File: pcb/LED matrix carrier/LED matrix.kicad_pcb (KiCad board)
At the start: 2 copper layers, 76.1 x 76.1 mm, 14 parts, among them J1 Conn_01x15_Pin, J2 Conn_01x15_Socket, J3 Conn_01x02_Pin, J4 Conn_01x02_Socket, J5 Conn_01x08_Socket, J6 Conn_01x08_Socket, J7 Conn_01x08_Socket, J8 Conn_01x08_Socket, U1 74HC594, U2 74HC594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

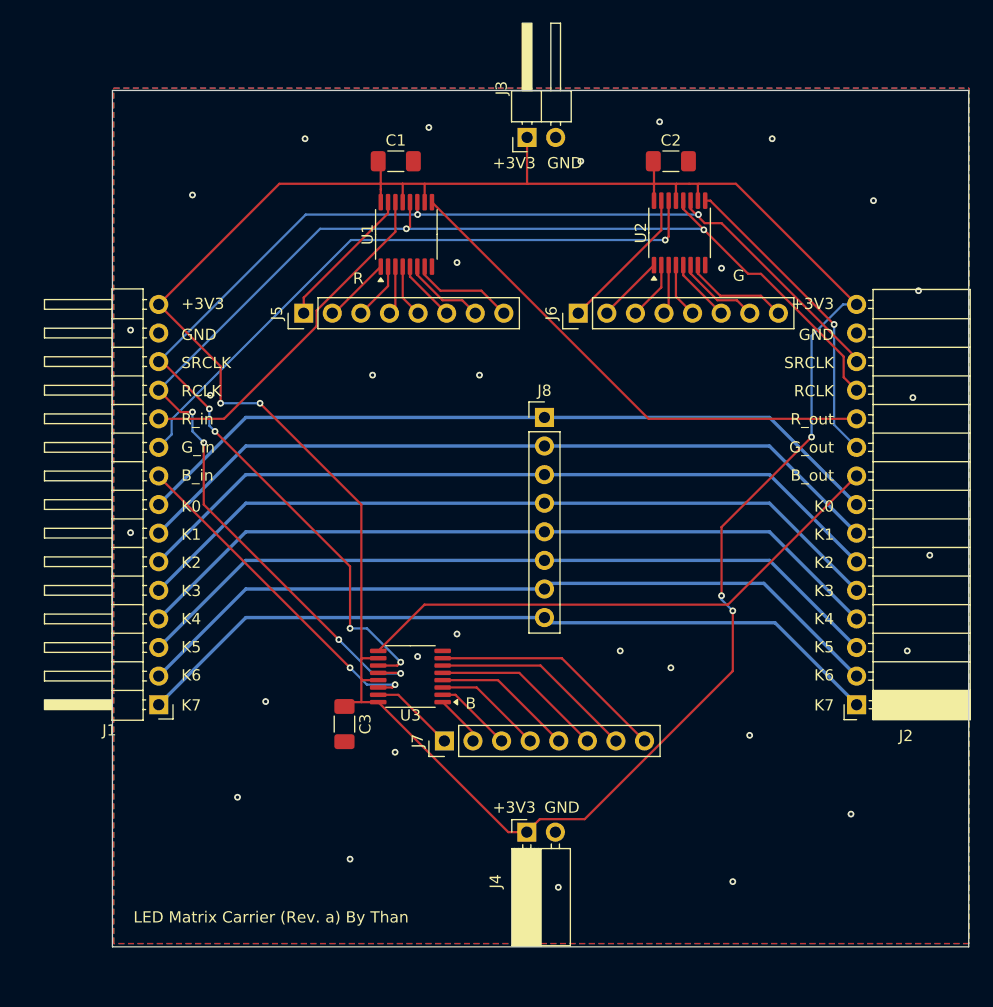
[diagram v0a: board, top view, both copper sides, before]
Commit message: export carrier pcb step model
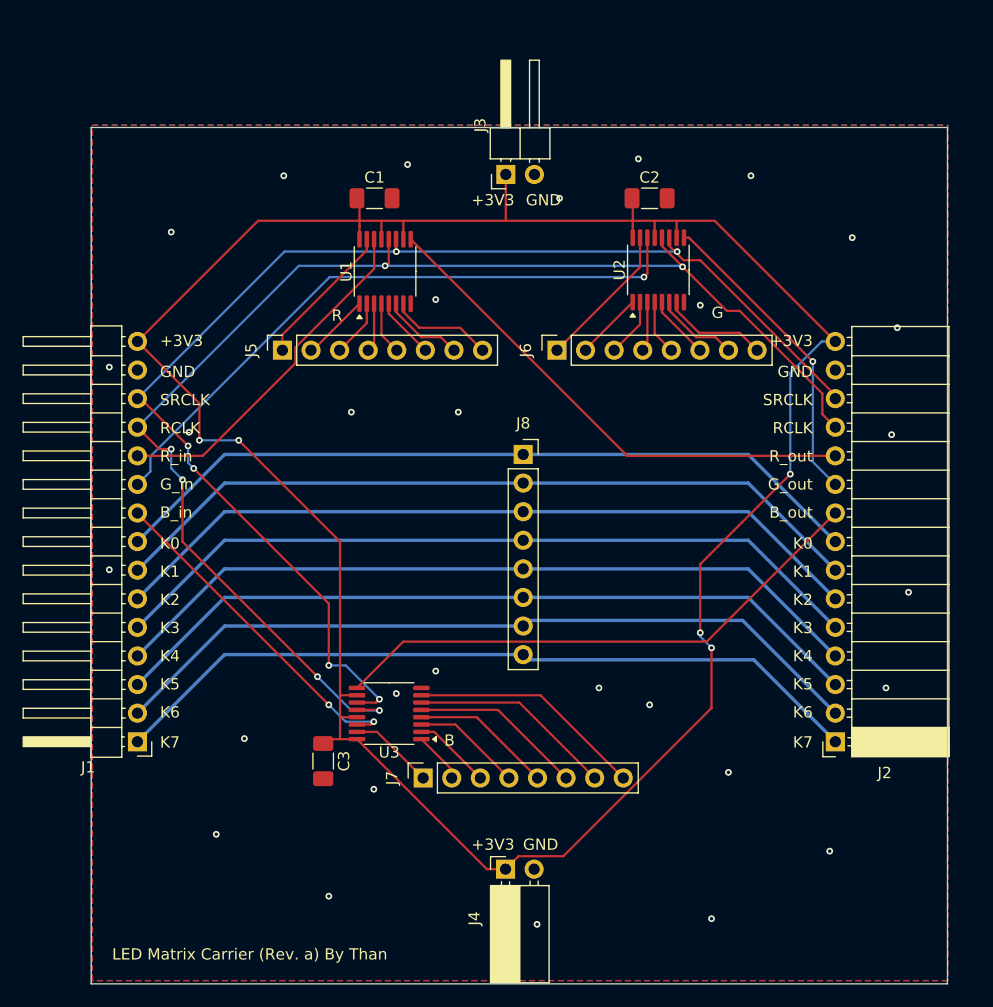
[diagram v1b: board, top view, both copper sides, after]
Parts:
- J5, J6, J7, J8: footprint Connector_PinHeader_2.54mm:PinHeader_1x08_P2.54mm_Vertical -> Connector_PinSocket_2.54mm:PinSocket_1x08_P2.54mm_Vertical
- moved U2 3.79 mm to (156.9, 51.7)
- moved J6 3.79 mm to (147.9, 58.8)
- moved C3 3.79 mm to (127.1, 95.3)
- moved J1 3.79 mm to (110.6, 93.6)
- moved J8 3.79 mm to (144.9, 68.0)
- moved U3 3.79 mm to (133.0, 91.1)
- moved J5 3.79 mm to (123.5, 58.8)
- moved J2 3.79 mm to (172.6, 93.6)
- moved J4 3.79 mm to (143.3, 104.9)
- moved J7 3.79 mm to (136.0, 96.8)
- moved C1 3.79 mm to (131.7, 45.3)
- moved C2 3.79 mm to (156.1, 45.3)
- moved J3 3.79 mm to (143.3, 43.2)
- moved U1 3.79 mm to (132.6, 51.8)

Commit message: fix wrong footprint/symbol
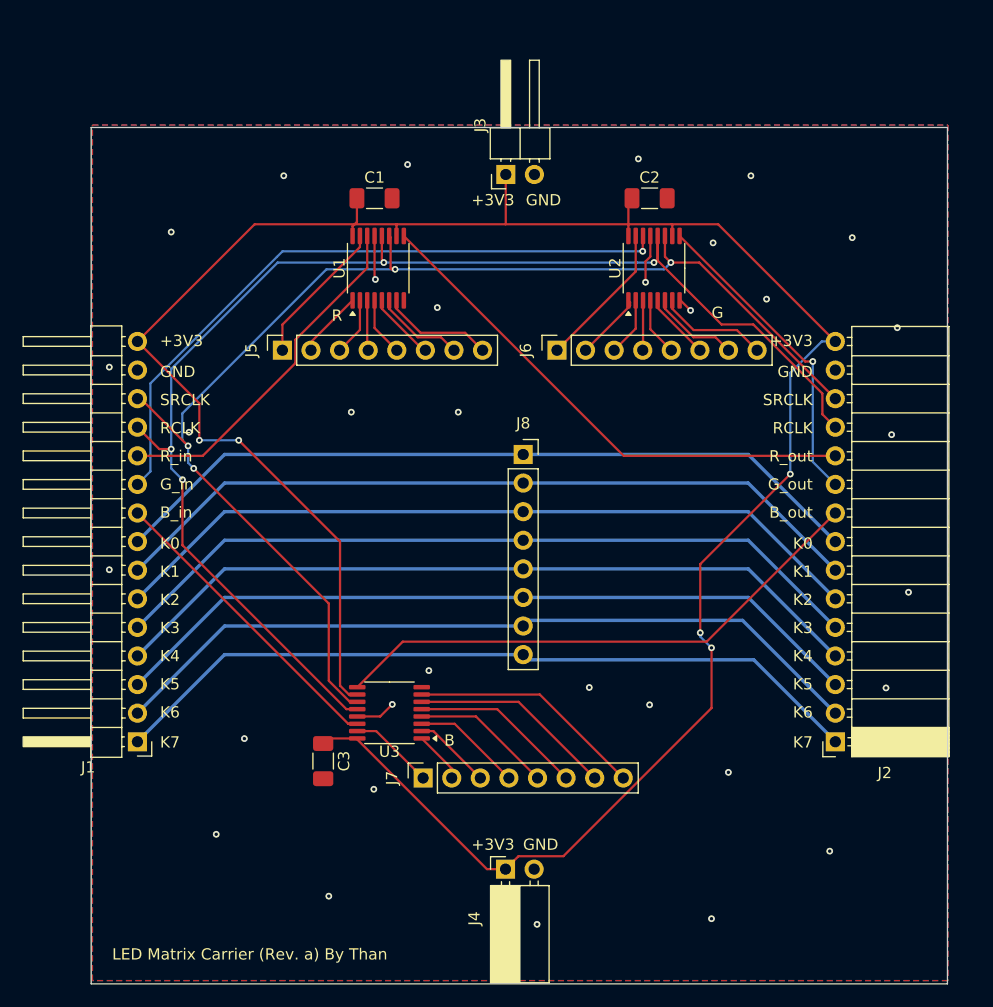
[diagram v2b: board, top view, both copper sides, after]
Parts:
- U1, U2, U3: value 74HC594 -> 74HC595
- moved U1 0.68 mm to (132.0, 51.5)
- moved U2 0.41 mm to (156.5, 51.5)
- moved U3 0.07 mm to (133.0, 91.0)
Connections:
- U1 pad 13: +3V3 -> GND
- U2 pad 13: +3V3 -> GND
- U3 pad 13: +3V3 -> GND
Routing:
- net GND: track 0.00 -> 13.1 mm, vias 30 -> 33
- net +3V3: track 220.1 -> 210.4 mm
- net /B_in: track 30.3 -> 27.3 mm, vias 2 -> 0
- net /G_in: track 57.0 -> 59.4 mm
- net /SRCLK: track 114.5 -> 113.5 mm, vias 6 -> 4
- net /matrix/R3: track 4.35 -> 5.21 mm
- net /matrix/R6: track 7.29 -> 8.02 mm
- net /R_out: track 45.7 -> 46.4 mm
- net /matrix/R7: track 9.18 -> 9.91 mm
- net /RCLK: track 119.0 -> 118.4 mm, vias 6 -> 4
- net /matrix/R5: track 5.49 -> 6.13 mm
- net /matrix/G3: track 4.44 -> 5.02 mm
- net /matrix/R4: track 4.70 -> 5.25 mm
